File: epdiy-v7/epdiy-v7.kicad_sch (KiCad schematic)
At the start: 117 parts, among them J1 USB_C_Receptacle_USB2.0, J2 EXTENSION_HEADER, J3 USB_HDR, J4 XF2M-3315-1A, J5 CONN_BAT, J6 8BIT_HEADER, J7 ESP_HDR, Q1 AO3401A, Q3 MMBT3904, Q4 MMBT3904, U1 RT9080-33GJ5, U10 ED060XC5, U11 TP4056, U2 PCA9535PW, U3 TPS651851RSLR, U4 USBLC6-2P6, U5 XC6206PxxxMR, U6 ED078KH6, U7 PCF8563T, U8 ESP32-S3-WROOM-1, U9 CH340C, Y1 32.768K

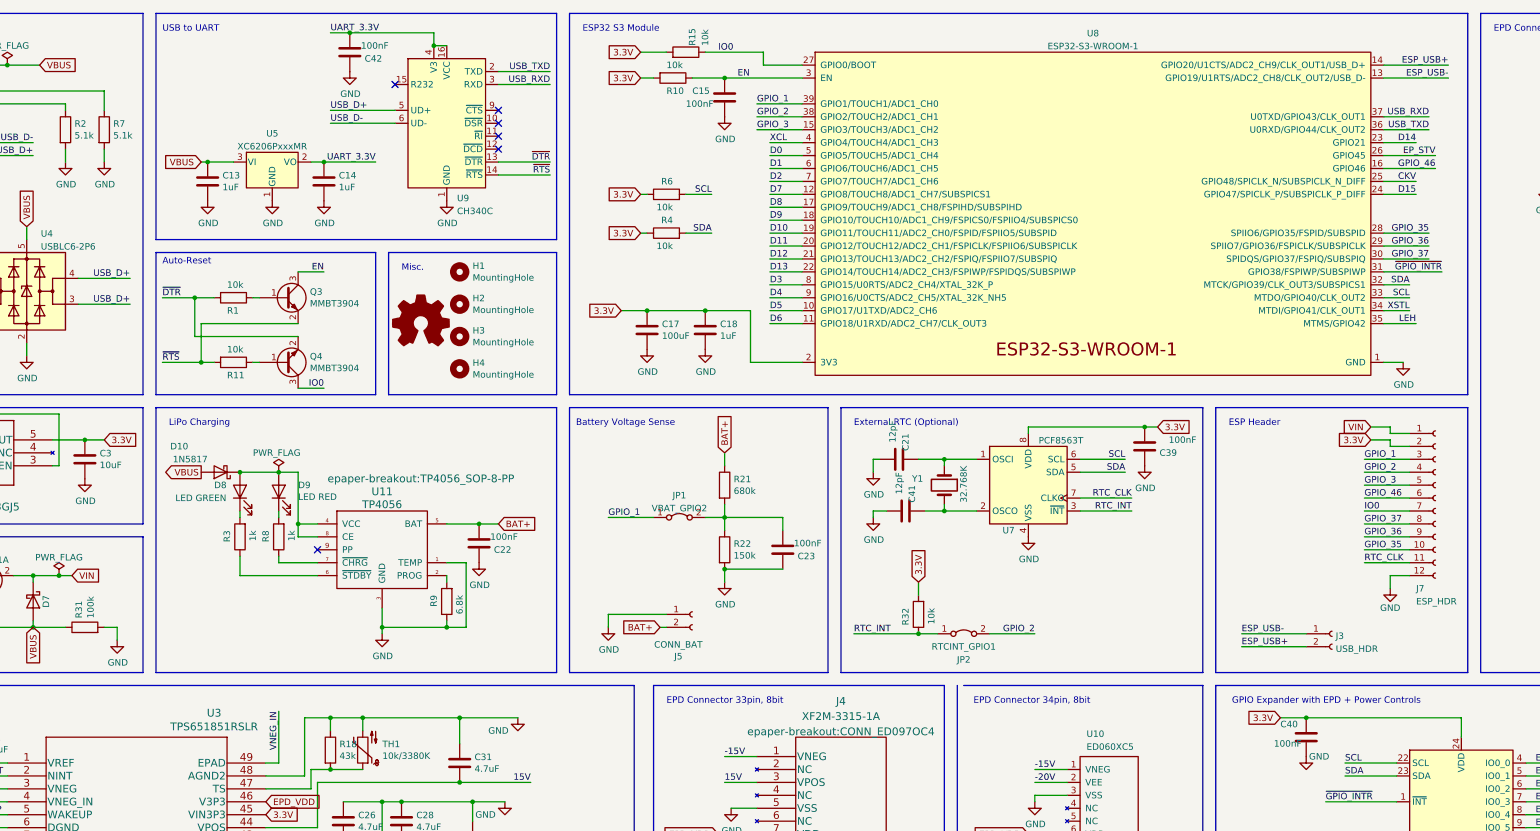
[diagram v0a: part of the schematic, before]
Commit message: Multiple changes. !!! Not for fabrication yet !!!
-USB-UART bridge removed-programming with USB only
-additional temperature and humidity sensor
-PCB layout modified - more consistent traces width, more 0.7/0.3 vias, teardrops etc
-jumpers removed and RX, TX signals routed to ext. pins
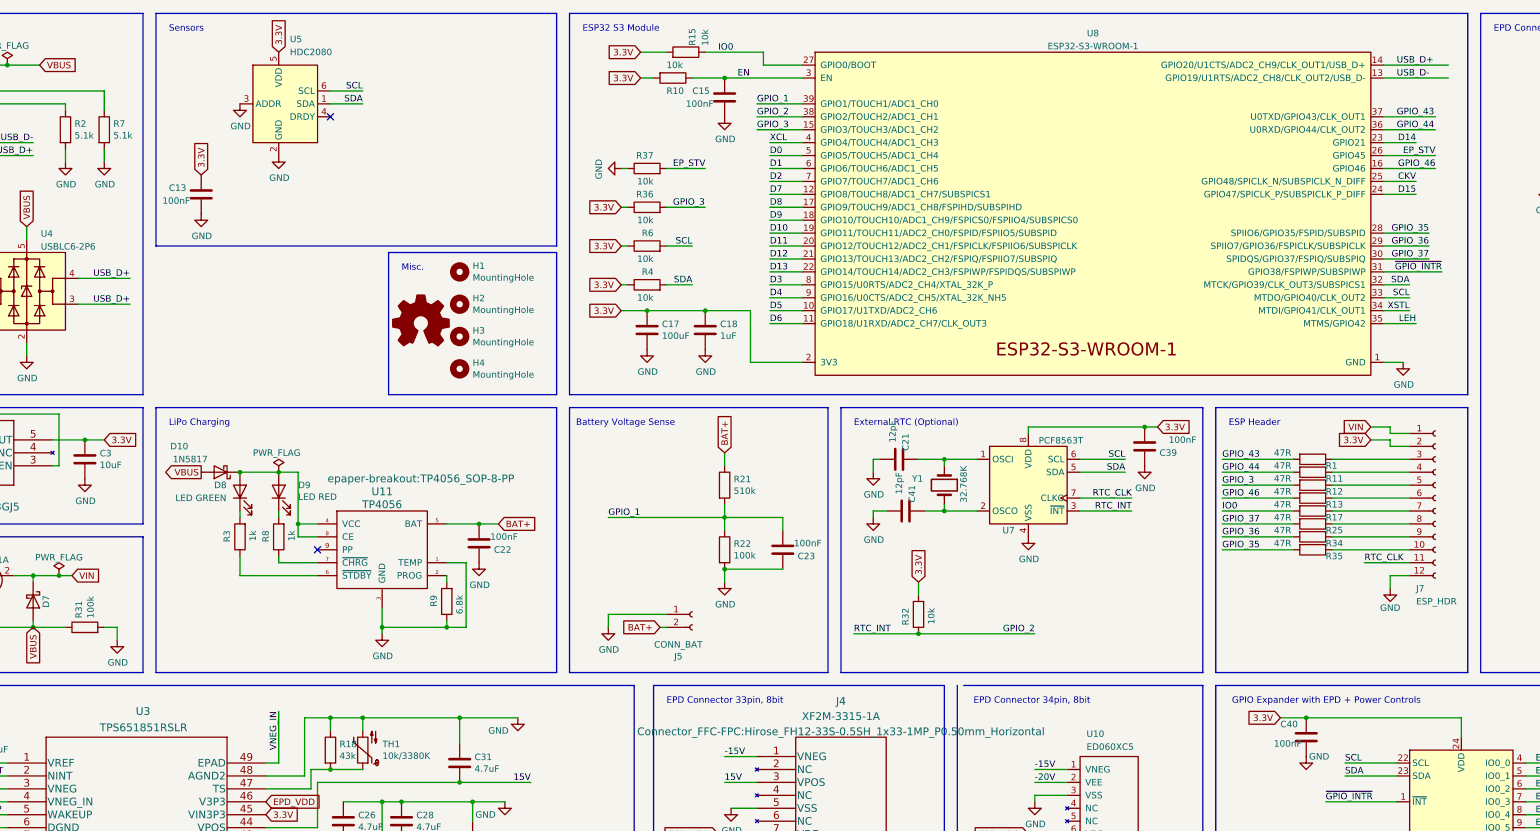
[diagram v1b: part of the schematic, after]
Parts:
- removed C14: 1uF, Capacitor_SMD:C_0805_2012Metric, symbol Device:C
- removed C42: 100nF, Capacitor_SMD:C_0805_2012Metric, symbol Device:C
- removed J3: USB_HDR, Connector_PinHeader_2.54mm:PinHeader_1x02_P2.54mm_Vertical, symbol Connector:Conn_01x02_Socket
- removed JP1: VBAT_GPIO2, Jumper:SolderJumper-2_P1.3mm_Bridged2Bar_Pad1.0x1.5mm, symbol Jumper:Jumper_2_Bridged
- removed JP2: RTCINT_GPIO1, Jumper:SolderJumper-2_P1.3mm_Bridged2Bar_Pad1.0x1.5mm, symbol Jumper:Jumper_2_Bridged
- removed Q3, Q4: MMBT3904, Package_TO_SOT_SMD:SOT-23, symbol Transistor_BJT:MMBT3904
- removed U5: XC6206PxxxMR, Package_TO_SOT_SMD:SOT-23-3, symbol Regulator_Linear:XC6206PxxxMR
- removed U9: CH340C, Package_SO:SOIC-16_3.9x9.9mm_P1.27mm, symbol Interface_USB:CH340C
- added R12, R13, R17, R25, R34, R35: 47R, Resistor_SMD:R_0603_1608Metric, symbol Device:R
- added R36, R37: 10k, Resistor_SMD:R_0603_1608Metric, symbol Device:R
- added U5: HDC2080, Package_SON:Texas_PWSON-N6, symbol Sensor_Humidity:HDC2080
- C13: value 1uF -> 100nF; footprint Capacitor_SMD:C_0805_2012Metric -> Capacitor_SMD:C_0603_1608Metric; LCSC C28323 -> C49678
- C21, C41: footprint Capacitor_SMD:C_0805_2012Metric -> Capacitor_SMD:C_0603_1608Metric; LCSC C1792 -> C38523
- C27, C33: LCSC C49217 -> C377773
- D1, D2, D3, D4, D5, D6, D7: LCSC C21353 -> C8598
- D8: footprint LED_SMD:LED_0805_2012Metric -> LED_SMD:LED_0603_1608Metric; LCSC C2297 -> C72043
- D9: footprint LED_SMD:LED_0805_2012Metric -> LED_SMD:LED_0603_1608Metric; LCSC C84256 -> C72038
- J4: footprint epaper-breakout:CONN_ED097OC4 -> Connector_FFC-FPC:Hirose_FH12-33S-0.5SH_1x33-1MP_P0.50mm_Horizontal; LCSC C231420 -> C597986
- R1, R11: value 10k -> 47R
- R21: value 680k -> 510k; LCSC C25822 -> C23192
- R22: value 150k -> 100k
- U2: LCSC C255606 -> C2652292
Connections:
- net ESP_USB+ is gone; now on net USB_D+: U8.14 (GPIO20/U1CTS/ADC2_CH9/CLK_OUT1/USB_D+)
- net ESP_USB- is gone; now on net USB_D-: U8.13 (GPIO19/U1RTS/ADC2_CH8/CLK_OUT2/USB_D-)
- net RTC_INT is gone; now on net GPIO_2: R32.1, U7.3 (~{INT})
- net ~{DTR} is gone; now on net GPIO_43: R1.2
- net ~{RTS} is gone; now on net GPIO_44: R11.2
- net 3.3V: now also C13.1, R36.1, U5.5 (VDD)
- net EP_STV: now also R37.2
- net GND: now also C13.2, R37.1, U5.2 (GND), U5.3 (ADDR); no longer C13.1
- net GPIO_1: now also C23.2, R21.2, R22.1; no longer J7.3 (Pin_3)
- net GPIO_2: no longer J7.4 (Pin_4)
- net GPIO_3: now also R12.2, R36.2; no longer J7.5 (Pin_5)
- net GPIO_35: now also R35.2; no longer J7.10 (Pin_10)
- net GPIO_36: now also R34.2; no longer J7.9 (Pin_9)
- net GPIO_37: now also R25.2; no longer J7.8 (Pin_8)
- net GPIO_46: now also R13.2; no longer J7.6 (Pin_6)
- net IO0: now also R17.2; no longer J7.7 (Pin_7)
- net SCL: now also U5.6 (SCL)
- net SDA: now also U5.1 (SDA)
- net VBUS: no longer C13.2
- net at R1.1: now also J7.3 (Pin_3)
- net at R11.1: now also J7.4 (Pin_4)
- net USB_RXD renamed GPIO_43
- net USB_TXD renamed GPIO_44
- new net: J7.8 (Pin_8), R25.1
- new net: J7.10 (Pin_10), R35.1
- new net: J7.5 (Pin_5), R12.1
- new net: J7.6 (Pin_6), R13.1
- new net: J7.7 (Pin_7), R17.1
- new net: J7.9 (Pin_9), R34.1
- no-connect marks 16 -> 12
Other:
- note added: "Sensors"
- note removed: "Auto-Reset"
- note removed: "USB to UART"
- moved on the sheet: R4, R6
